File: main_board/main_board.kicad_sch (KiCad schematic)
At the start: 47 parts, among them J1 USB Port, J2 I2C, J3 LED, J4 Left_Mic, J5 Left_Speaker, J6 Right_Mic, J7 Right_Speaker, J8 I2C, Q1 MMBT3904, Q2 MMBT3904, SW1 SW_Push, SW2 SW_Push, SW3 SW_Push, U1 AMS1117-3.3, U2 CH340K, U4 Headphone Jack, U7 AMS1117-3.3, U8 ESP32-WROOM-32E

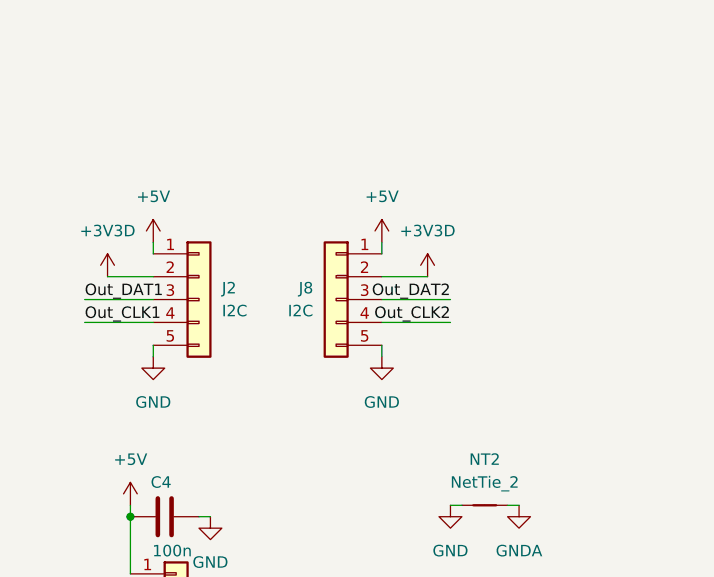
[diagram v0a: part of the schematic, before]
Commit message: fix: missing I2C pullup resistors
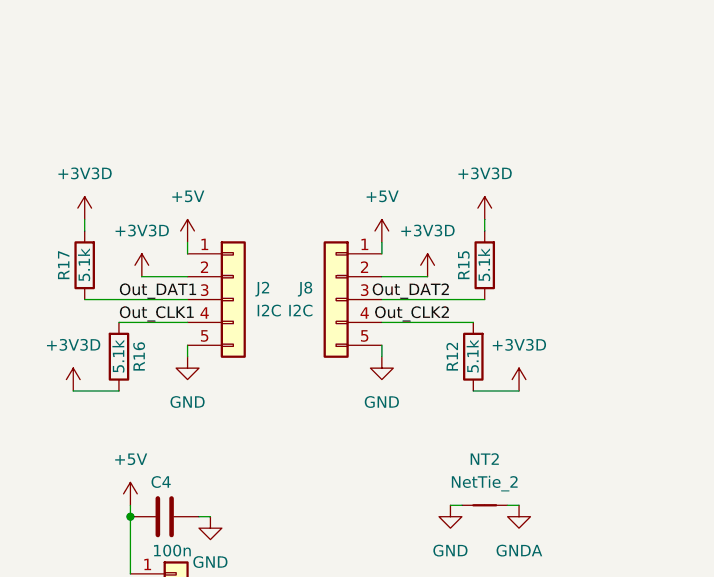
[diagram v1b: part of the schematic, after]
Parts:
- added R12, R15, R16, R17: 5.1k, Resistor_SMD:R_0402_1005Metric, symbol Device:R
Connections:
- net +3V3D: now also R12.1, R15.2, R16.1, R17.2
- net Out_CLK1: now also R16.2
- net Out_CLK2: now also R12.2
- net Out_DAT1: now also R17.1
- net Out_DAT2: now also R15.1
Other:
- moved on the sheet: J2

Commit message: finish v1.0
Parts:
- removed C7, C8: 100n, Capacitor_SMD:C_0402_1005Metric, symbol Device:C
- added R18, R19: 1k, Resistor_SMD:R_0402_1005Metric, symbol Device:R
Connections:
- net GPIO0: now also R18.2; no longer SW1.2
- net MCU_EN: now also R19.2; no longer SW2.2
- new net: R19.1, SW2.2
- new net: R18.1, SW1.2
- no-connect marks 4 -> 8
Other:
- moved on the sheet: SW1, SW2

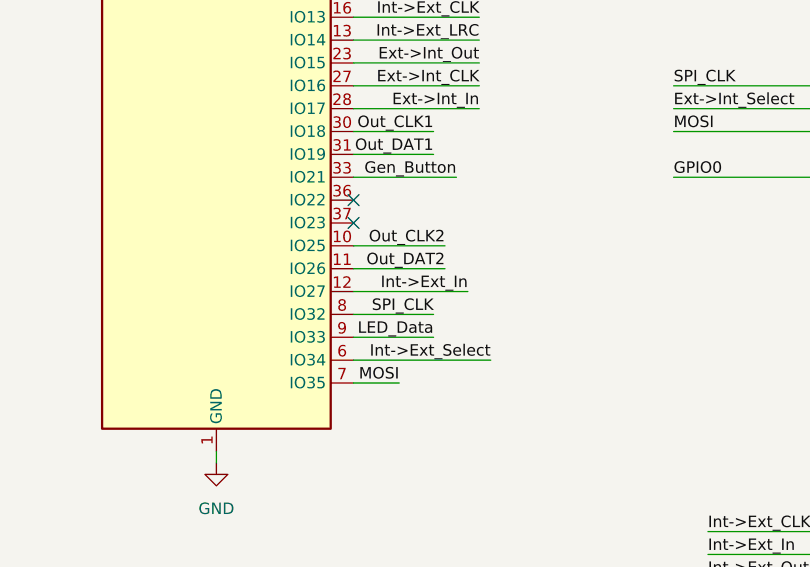
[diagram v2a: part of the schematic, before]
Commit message: reroute SPI (non output pin issue)
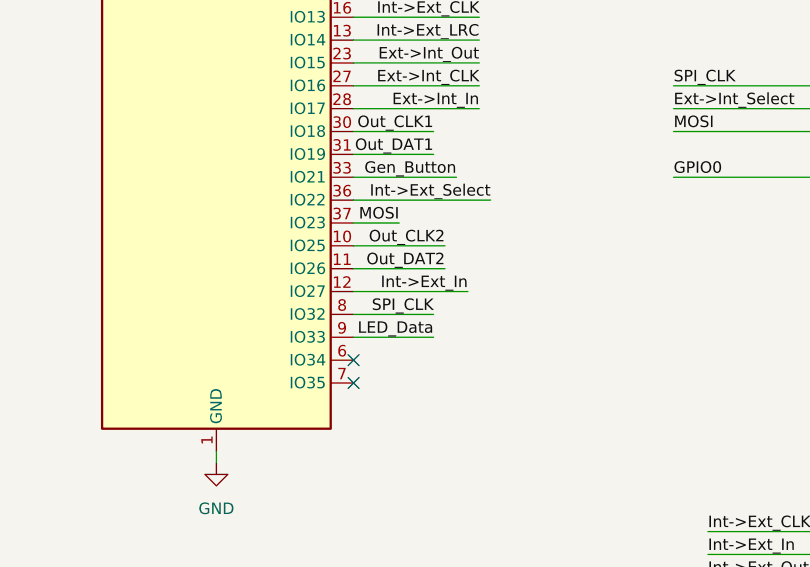
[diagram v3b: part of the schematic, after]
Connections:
- net Int->Ext_Select: now also U8.36 (IO22); no longer U8.6 (IO34)
- net MOSI: now also U8.37 (IO23); no longer U8.7 (IO35)
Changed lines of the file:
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@@
-	)
-	(no_connect
-		(at 184.15 82.55)
 	)
 	(no_connect
@@
 	)
 	(no_connect
-		(at 184.15 80.01)
+		(at 40.64 53.34)
 	)
 	(no_connect
-		(at 40.64 53.34)
+		(at 184.15 100.33)
+	)
+	(no_connect
+		(at 184.15 97.79)
 	)
 	(no_connect
@@
 	(wire
 		(pts
+			(xy 184.15 82.55) (xy 189.23 82.55)
+		)
+		(stroke
+			(width 0)
+			(type default)
+		)
+	)
+	(wire
+		(pts
 			(xy 24.13 162.56) (xy 19.05 162.56)
 		)
@@
 	(wire
 		(pts
-			(xy 199.39 97.79) (xy 184.15 97.79)
-		)
-		(stroke
-			(width 0)
-			(type default)
-		)
-	)
-	(wire
-		(pts
 			(xy 60.96 175.26) (xy 62.23 175.26)
 		)
@@
 	(wire
 		(pts
+			(xy 199.39 80.01) (xy 184.15 80.01)
+		)
+		(stroke
+			(width 0)
+			(type default)
+		)
+	)
+	(wire
+		(pts
 			(xy 53.34 146.05) (xy 53.34 147.32)
 		)
@@
 		(pts
 			(xy 68.58 175.26) (xy 67.31 175.26)
-		)
-		(stroke
-			(width 0)
-			(type default)
-		)
-	)
-	(wire
-		(pts
-			(xy 189.23 100.33) (xy 184.15 100.33)
 		)
 		(stroke
@@
 		)
 	)
-	(label "Int->Ext_Select"
-		(at 199.39 97.79 180)
-		(effects
-			(font
-				(size 1.27 1.27)
-			)
-			(justify right bottom)
-		)
-	)
 	(label "Headset_Right"
 		(at 262.89 93.98 180)
@@
 		)
 	)
+	(label "MOSI"
+		(at 189.23 82.55 180)
+		(effects
+			(font
+				(size 1.27 1.27)
+			)
+			(justify right bottom)
+		)
+	)
 	(label "LED_Data"
 		(at 16.51 185.42 0)
@@
 		)
 	)
+	(label "Int->Ext_Select"
+		(at 199.39 80.01 180)
+		(effects
+			(font
+				(size 1.27 1.27)
+			)
+			(justify right bottom)
+		)
+	)
 	(label "MCU_EN"
 		(at 142.24 76.2 180)
@@
 		(effects
 			(font
-				(size 1.27 1.27)
-			)
-			(justify right bottom)
-		)
-	)
-	(label "MOSI"
-		(at 189.23 100.33 180)
-		(effects
-			(font
